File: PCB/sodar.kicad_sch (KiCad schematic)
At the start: 30 parts, among them U1 TC78H621FNG, U10 TC78H621FNG, U11 TC78H621FNG, U2 QBLP680-RGB1, U3 TC78H621FNG, U4 TC78H621FNG, U5 TC78H621FNG, U6 TC78H621FNG, U7 TC78H621FNG, U8 TC78H621FNG, U9 TC78H621FNG

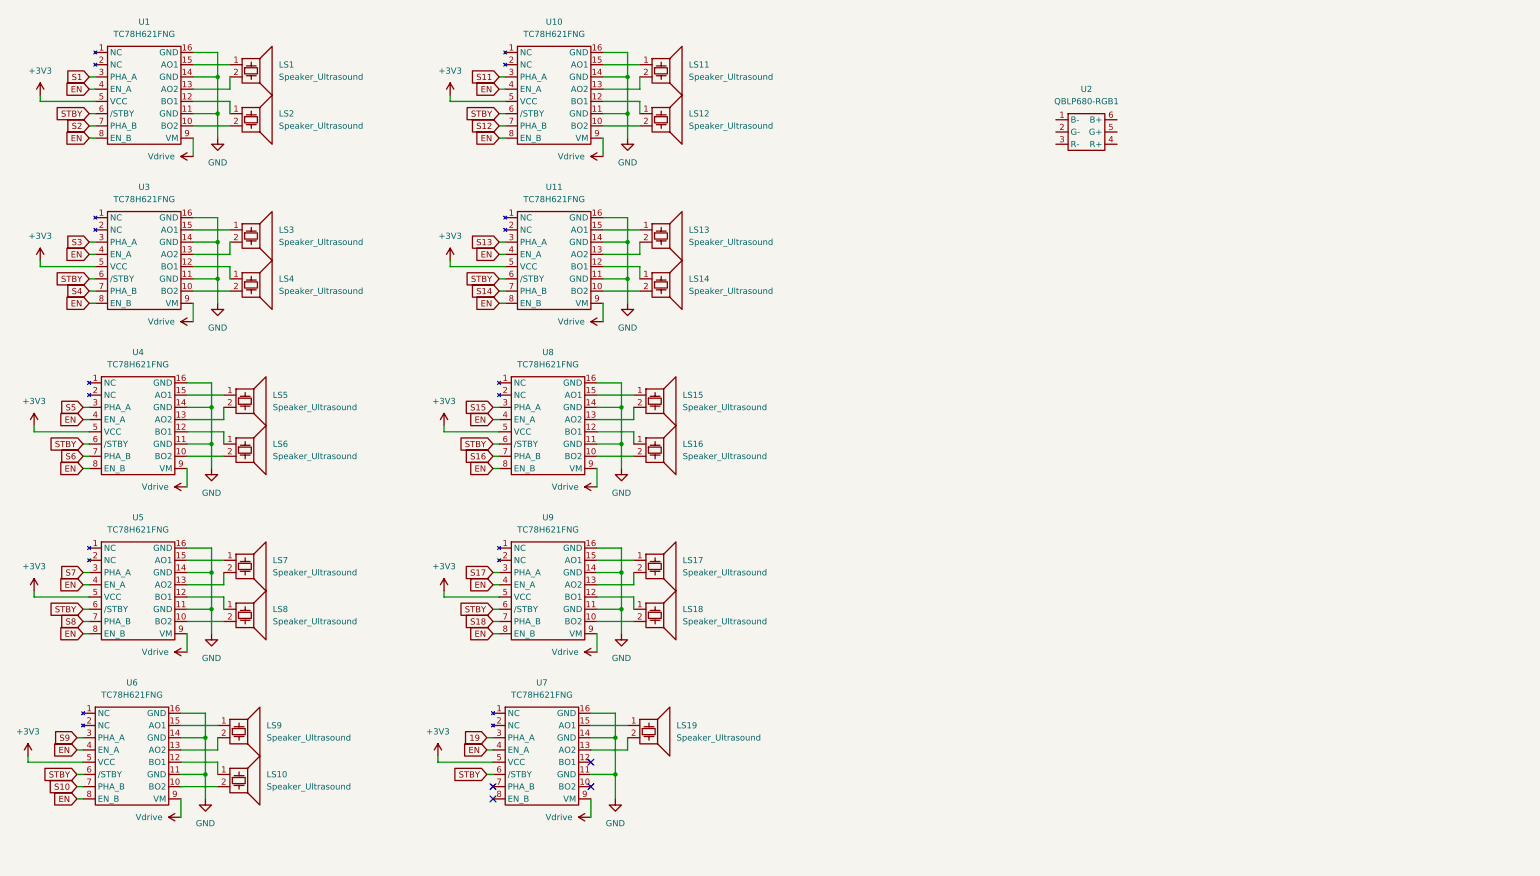
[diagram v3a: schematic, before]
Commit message: Added capacitors to the drivers & Added receiver
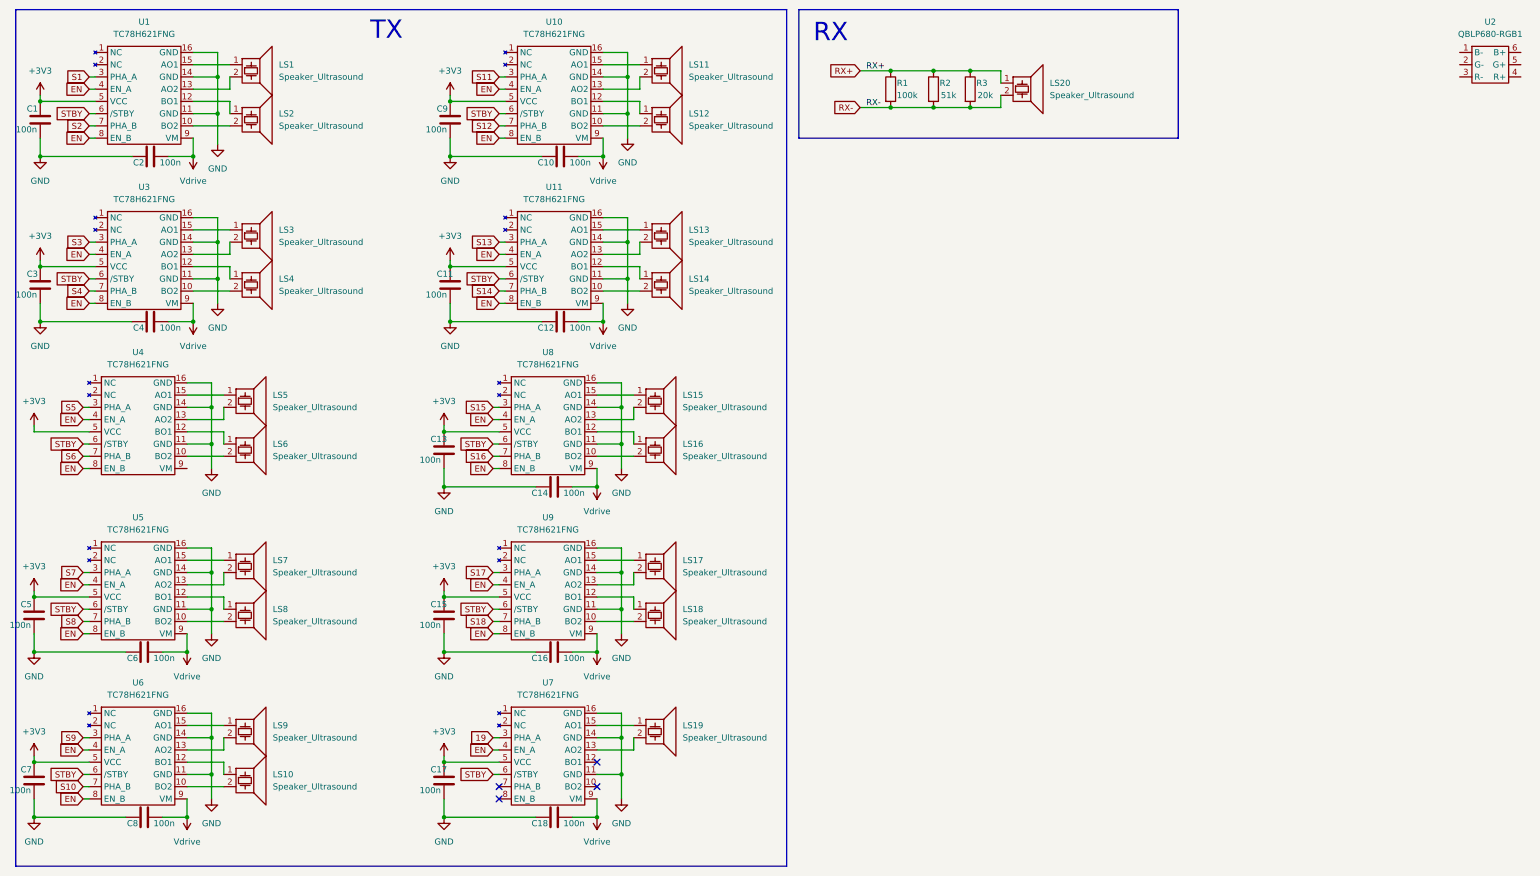
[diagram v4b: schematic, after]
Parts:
- added C1, C10, C11, C12, C13, C14, C15, C16, C17, C18, C2, C3, C4, C5, C6, C7, C8, C9: 100n, symbol Device:C
- added LS20: Speaker_Ultrasound, footprints:MCUSR16A39S12RO, symbol Device:Speaker_Ultrasound
- added R1: 100k, symbol Device:R
- added R2: 51k, symbol Device:R
- added R3: 20k, symbol Device:R
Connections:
- net +3V3: now also C1.1, C11.1, C13.1, C15.1, C17.1, C3.1, C5.1, C7.1, C9.1
- net GND: now also C1.2, C10.1, C11.2, C12.1, C13.2, C14.1, C15.2, C16.1, C17.2, C18.1, C2.1, C3.2, C4.1, C5.2, C6.1, C7.2, C8.1, C9.2
- net Vdrive: now also C10.2, C12.2, C14.2, C16.2, C18.2, C2.2, C4.2, C6.2, C8.2; no longer U4.9 (VM)
- new net RX+: LS20.1, R1.1, R2.1, R3.1
- new net RX-: LS20.2, R1.2, R2.2, R3.2
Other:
- note added: "RX"
- note added: "TX"
- moved on the sheet: LS10, LS19, LS9, U2, U6, U7

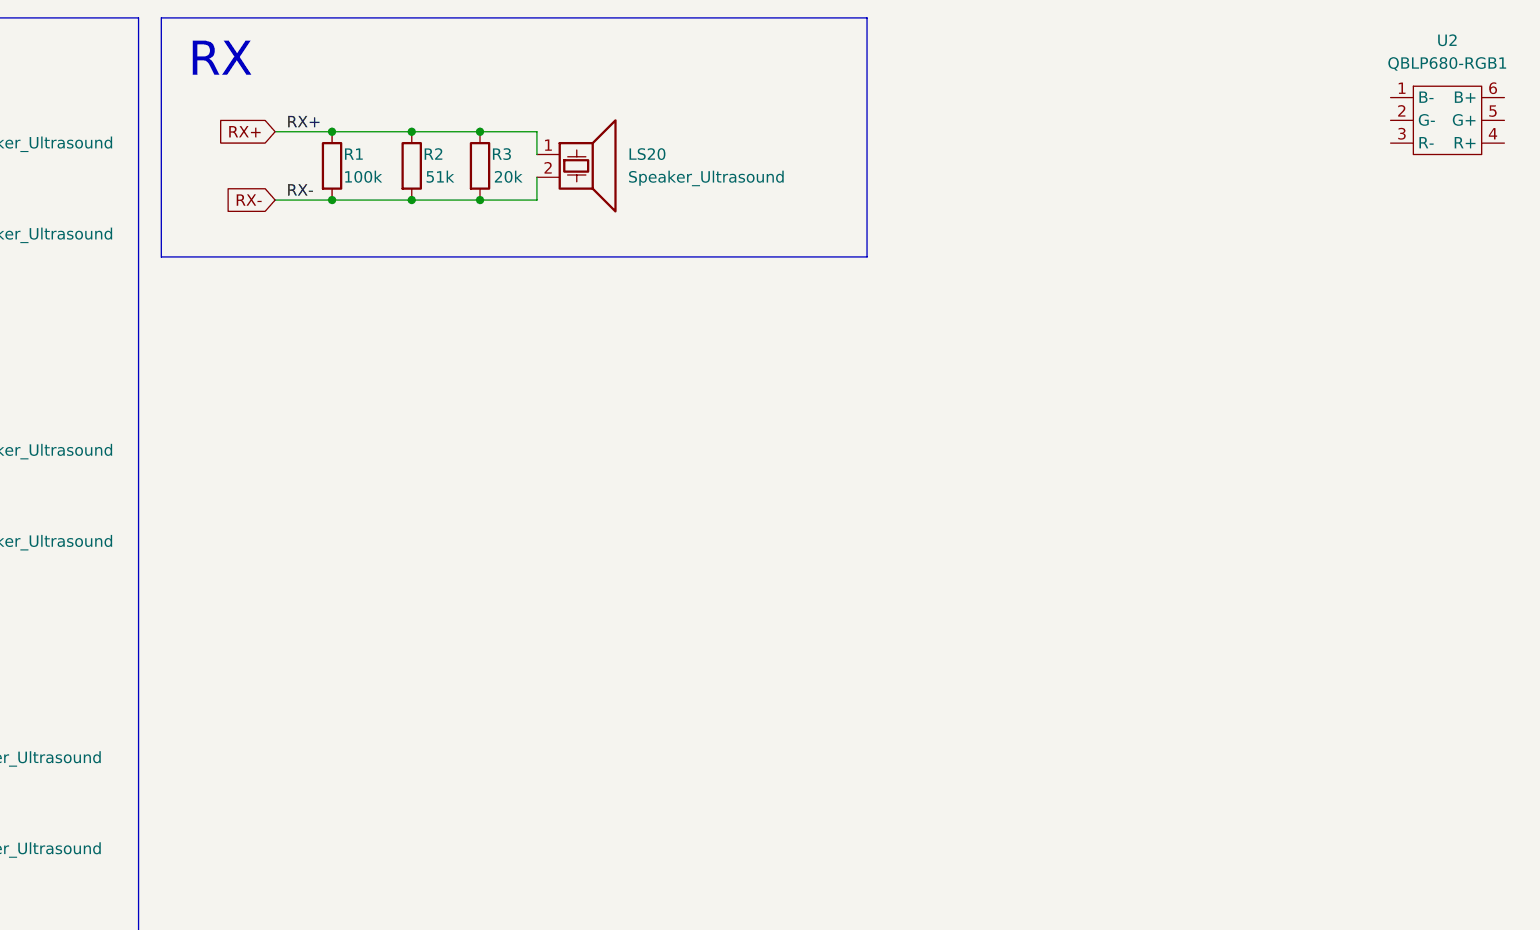
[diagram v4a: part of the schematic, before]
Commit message: Added Pin header
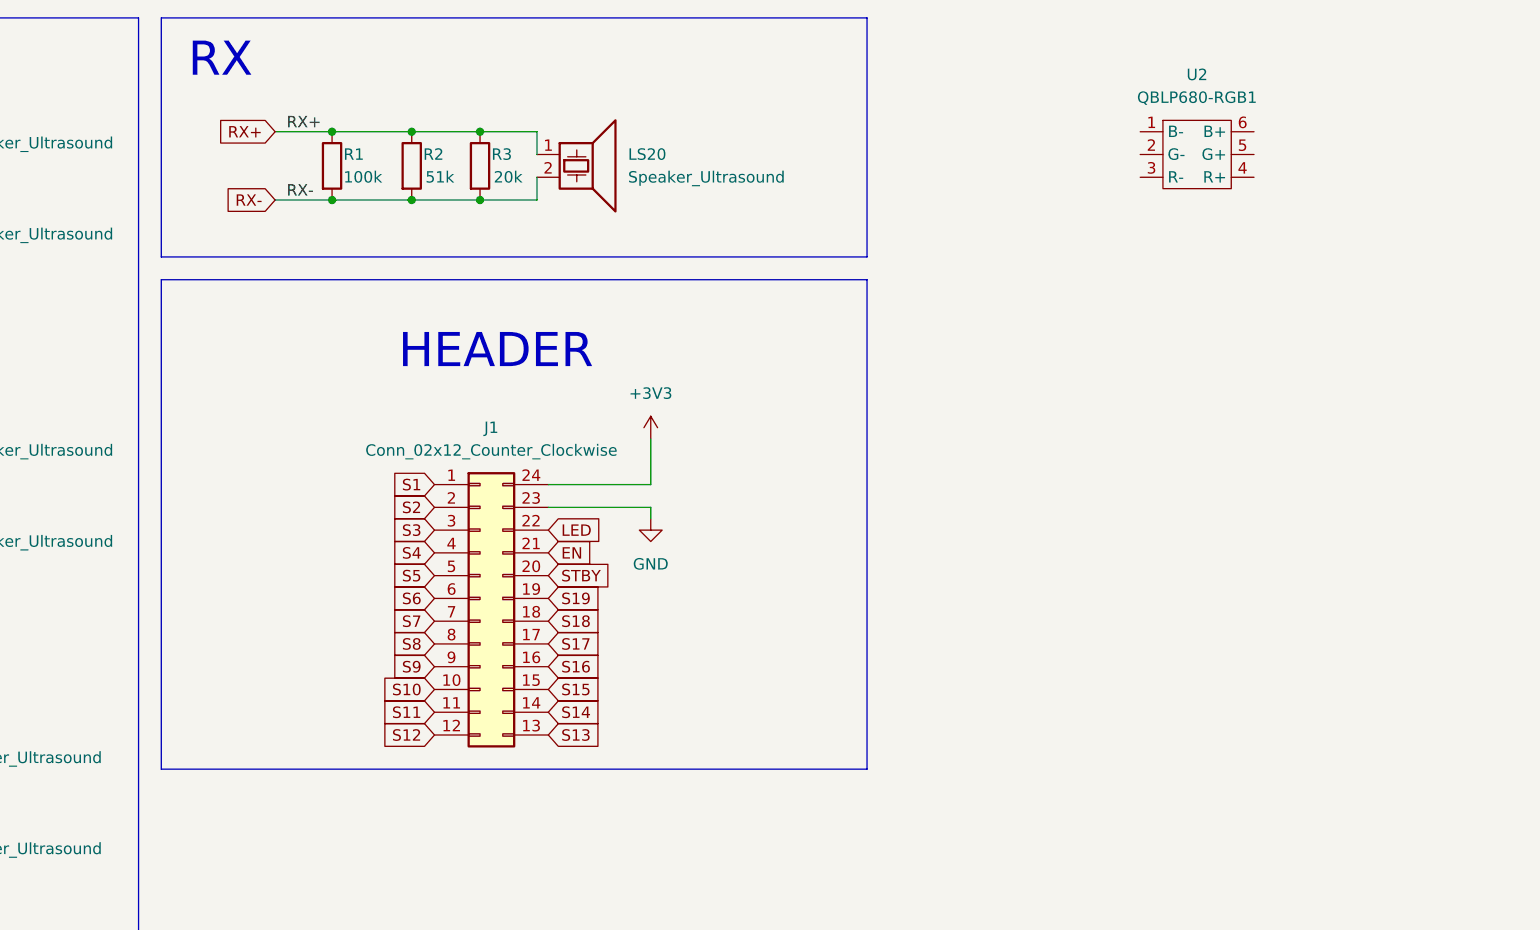
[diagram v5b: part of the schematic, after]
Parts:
- added J1: Conn_02x12_Counter_Clockwise, symbol Connector_Generic:Conn_02x12_Counter_Clockwise
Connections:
- net +3V3: now also J1.24 (Pin_24)
- net EN: now also J1.21 (Pin_21)
- net GND: now also J1.23 (Pin_23)
- net S1: now also J1.1 (Pin_1)
- net S10: now also J1.10 (Pin_10)
- net S11: now also J1.11 (Pin_11)
- net S12: now also J1.12 (Pin_12)
- net S13: now also J1.13 (Pin_13)
- net S14: now also J1.14 (Pin_14)
- net S15: now also J1.15 (Pin_15)
- net S16: now also J1.16 (Pin_16)
- net S17: now also J1.17 (Pin_17)
- net S18: now also J1.18 (Pin_18)
- net S2: now also J1.2 (Pin_2)
- net S3: now also J1.3 (Pin_3)
- net S4: now also J1.4 (Pin_4)
- net S5: now also J1.5 (Pin_5)
- net S6: now also J1.6 (Pin_6)
- net S7: now also J1.7 (Pin_7)
- net S8: now also J1.8 (Pin_8)
- net S9: now also J1.9 (Pin_9)
- net STBY: now also J1.20 (Pin_20)
- new net LED: J1.22 (Pin_22)
- new net S19: J1.19 (Pin_19)
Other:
- note added: "HEADER"
- moved on the sheet: U2

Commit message: Added LEDs to the schematics - PWR EN STBY LED PHA
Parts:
- removed U2: QBLP680-RGB1, footprints:QBLP680-RGB1, symbol symbols:QBLP680-RGB1
- added C19, C20: 100n, symbol Device:C
- added D1, D2, D3, D4: QBLP680-RGB1, footprints:QBLP680-RGB1, symbol symbols:QBLP680-RGB1
- added R4, R5, R8: 43, symbol Device:R
- added R6, R7: 100, symbol Device:R
- added R9: 2k, symbol Device:R
- renumbered U7 to U10, U3 to U2, U4 to U3, U5 to U4, U6 to U5, U10 to U6, U11 to U7
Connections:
- net 19 is gone; now on net S19: U10.3 (PHA_A)
- net +3V3: now also C19.1, D1.5 (G+)
- net EN: now also U10.8 (EN_B), D2.4 (R+)
- net GND: now also C19.2, C20.1, R4.1, R5.1, R6.1, R8.1
- net LED: now also D3.6 (B+)
- net S19: now also U10.7 (PHA_B)
- net STBY: now also D1.6 (B+)
- net Vdrive: now also U3.9 (VM), C20.2
- net PHA_LED2: now reaches U10.10 (BO2)
- net PHA_LED2: now also D4.3 (R-), D4.6 (B+)
- net PHA_LED1: now reaches U10.12 (BO1)
- net PHA_LED1: now also R9.1
- new net: D1.1 (B-), R4.2
- new net: D1.2 (G-), R5.2
- new net: D3.1 (B-), R8.2
- new net: R6.2, R7.1
- new net: D2.3 (R-), R7.2
- new net: D4.1 (B-), D4.4 (R+), R9.2
- no-connect marks 4 -> 12
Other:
- note added: "EN"
- note added: "LED"
- note added: "LEDs"
- note added: "PHA"
- note added: "PWR & STBY"
- moved on the sheet: LS10, LS15, LS16, LS17, LS18, LS19, LS5, LS6, LS7, LS8, LS9

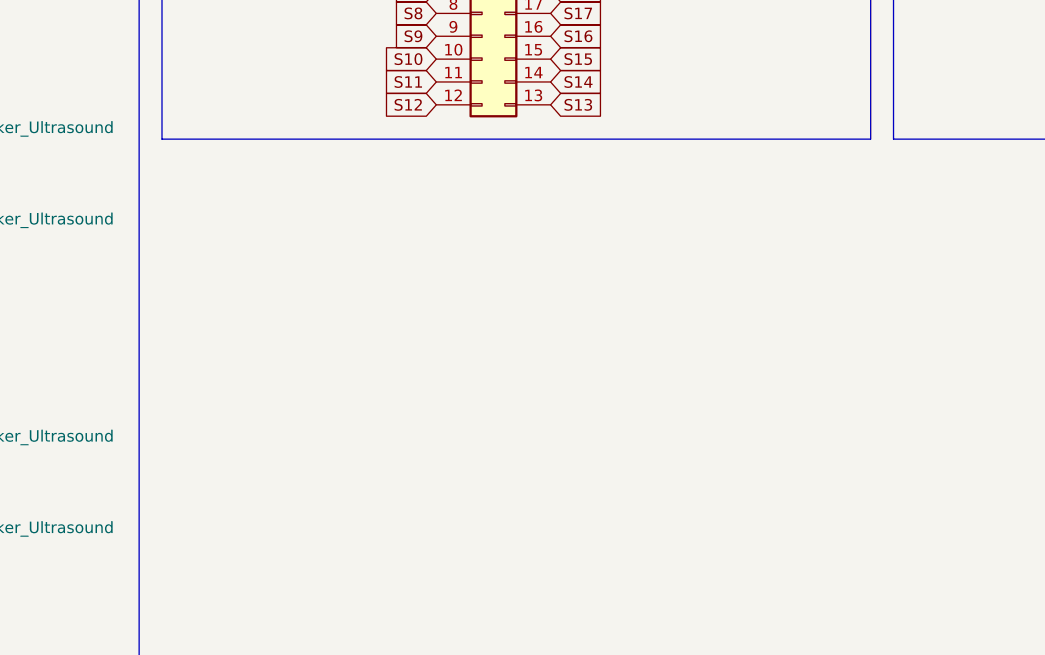
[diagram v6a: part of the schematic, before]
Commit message: Added Screw terminal & capacitors to the schematics
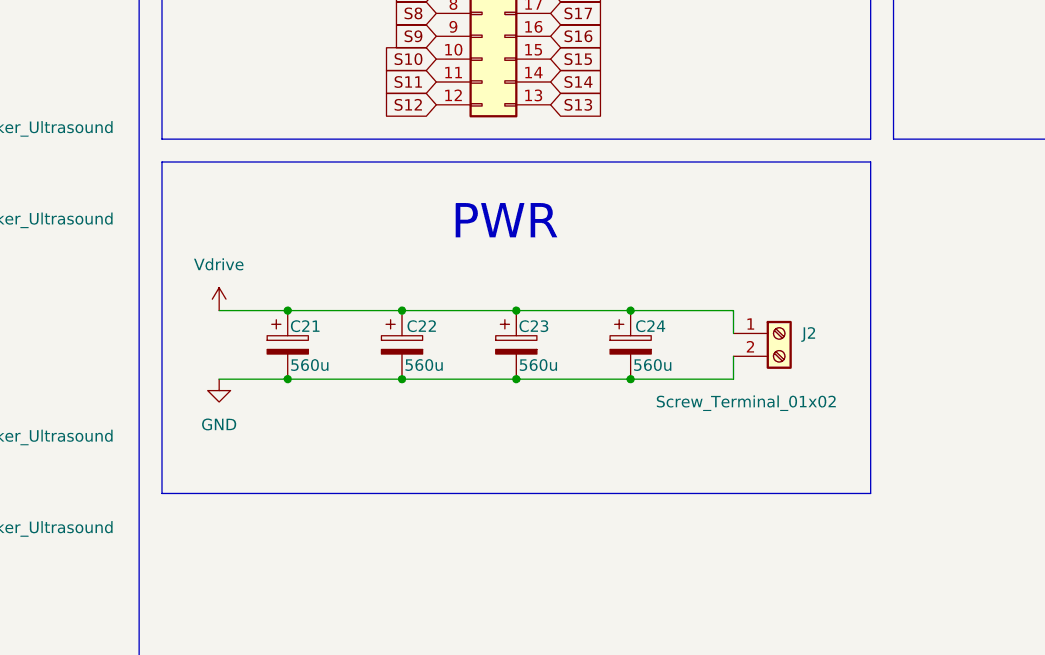
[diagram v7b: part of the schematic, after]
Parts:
- added C21, C22, C23, C24: 560u, symbol Device:C_Polarized
- added J2: Screw_Terminal_01x02, TerminalBlock_4Ucon:TerminalBlock_4Ucon_1x02_P3.50mm_Horizontal, symbol Connector:Screw_Terminal_01x02
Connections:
- net GND: now also C21.2, C22.2, C23.2, C24.2, J2.2 (Pin_2)
- net Vdrive: now also C21.1, C22.1, C23.1, C24.1, J2.1 (Pin_1)
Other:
- note added: "PWR"
